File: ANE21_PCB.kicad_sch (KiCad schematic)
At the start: 23 parts, among them J1 Conn_02x07_Odd_Even, J2 Conn_01x03, J3 Conn_01x03, J4 THD-20-R, U1 74LVC1G07SE-7, U2 74LVC1G07SE-7

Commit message: Added footprints and symbols
Could not find -on SnapEDA- MCWR06X3322FTL, MCMR06X3162FTL and USB-A-S-VT.
Power load switch NCP380HSN05AAT1G only had footprint on SnapEDA, no symbol.
Need to update HMDI footprint and symbol to correct one.
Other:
- sheet CM4_GPIO ( Ethernet, GPIO, SDCARD) renamed Main
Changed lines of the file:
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@@
 			(color 255 255 255 0.0000)
 		)
-		(property "Sheetname" "CM4_GPIO ( Ethernet, GPIO, SDCARD)"
+		(property "Sheetname" "Main"
 			(at 213.36 127 0)
 			(effects

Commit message: Added footprints for PCIe and added busses for PCIe and Ethernet
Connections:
- net SYNC_IN: no longer Module?.16 (Ethernet_SYNC_IN(1.8v))
- net SYNC_OUT: no longer Module?.18 (Ethernet_SYNC_OUT(1.8v))
- no-connect marks 6 -> 8
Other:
- sheet Main renamed CM4_LowSpeed
- added sheet Ethernet (Ethernet.kicad_sch)

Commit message: Moved PCIe psu to global psu schematic
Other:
- removed sheet PCIe-connector
- sheet CM4_HighSpeed ports: added none; removed PCIE_CLK_N, PCIE_CLK_P, PCIE_CLK_nREQ, PCIE_RX_N, PCIE_RX_P, PCIE_TX_N, PCIE_TX_P, PCIE_nRST
- note added: "Connectors ------- Ethernet 40way RPI Jumpers"
- note added: "Connectors ------- HDMI 0 CSI 0 CSI 1"
- note removed: "Connector ------ PCIe x1"
- note removed: "Connectors ------- Ethernet SDCARD 40way RPI Jumpers"
- note removed: "Connectors ------- HDMI 0 HDMI 1 CSI 0 CSI 1 DSI 0 DSI 1"

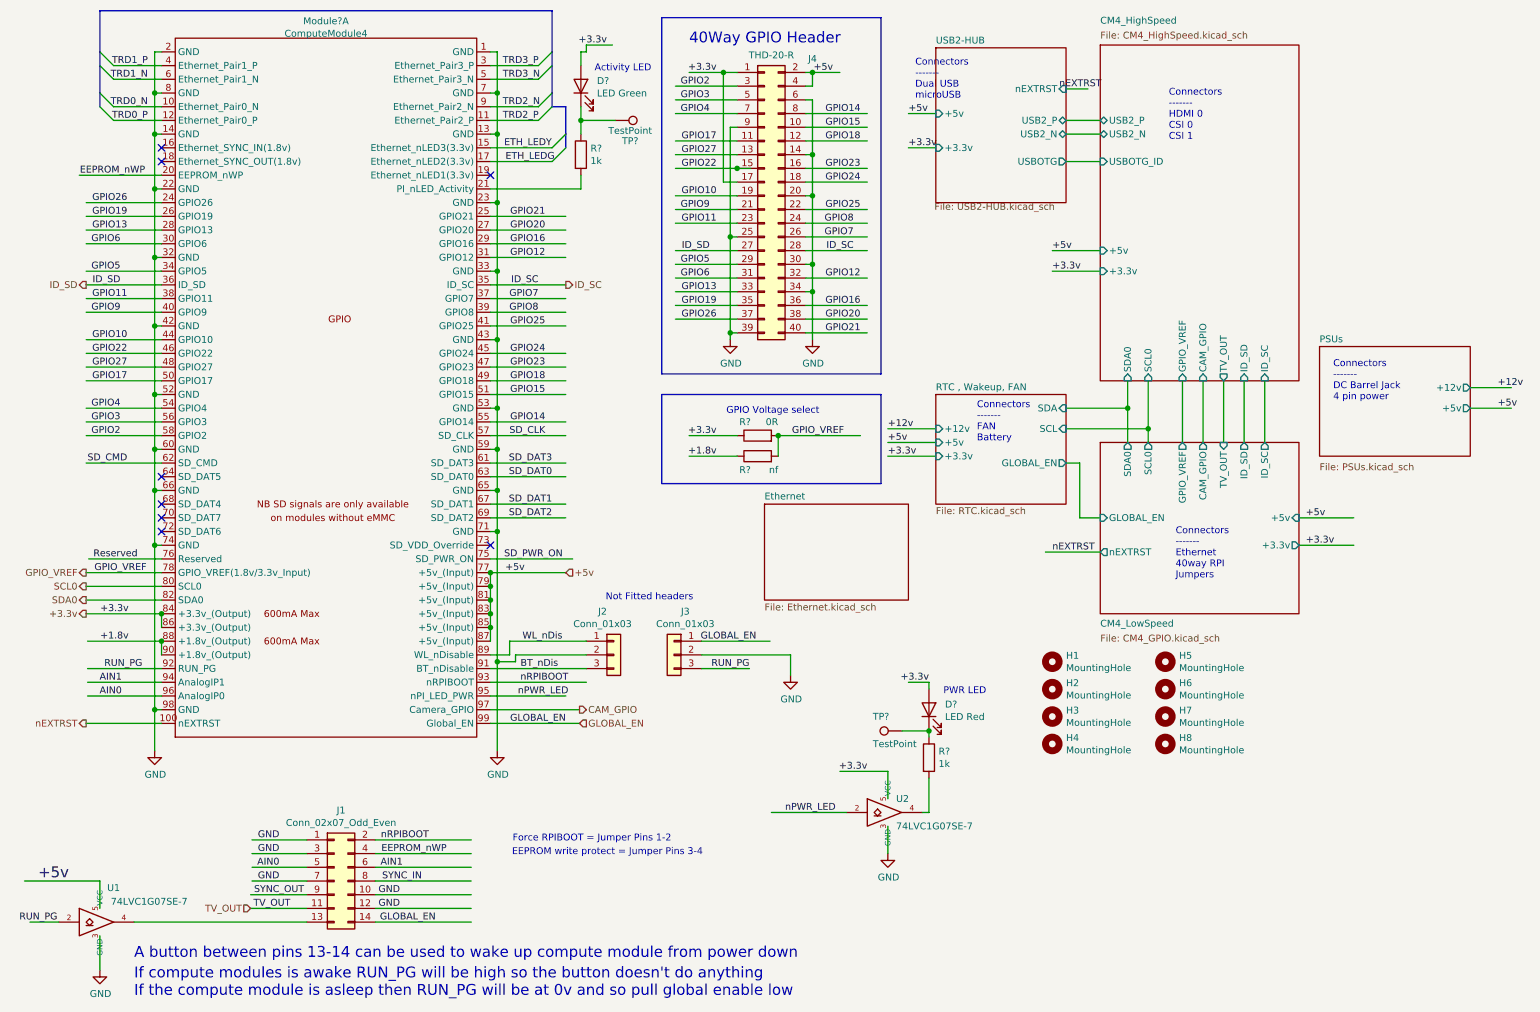
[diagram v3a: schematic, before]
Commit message: Cleaned up schematics and added gnds and no-connects
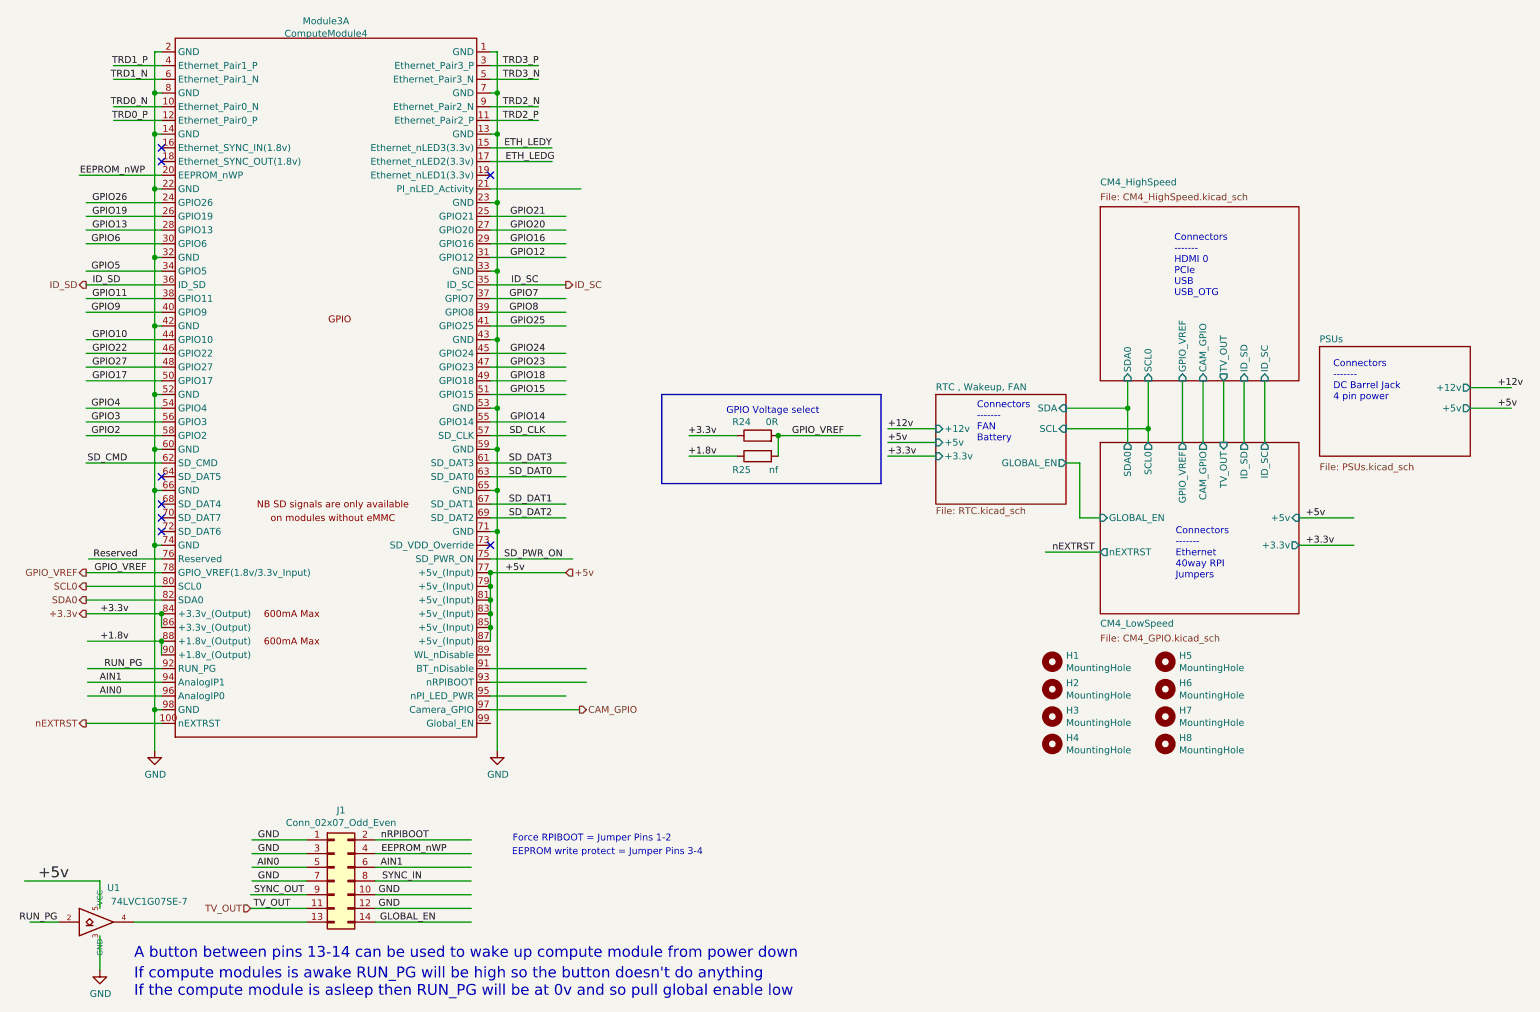
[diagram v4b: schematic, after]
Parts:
- removed D?: LED Green, LED_SMD:LED_0603_1608Metric, symbol Device:LED
- removed D?: LED Red, LED_SMD:LED_0603_1608Metric, symbol Device:LED
- removed J2, J3: Conn_01x03, Connector_PinHeader_2.54mm:PinHeader_1x03_P2.54mm_Vertical, symbol Connector_Generic:Conn_01x03
- removed J4: THD-20-R, Connector_PinHeader_2.54mm:PinHeader_2x20_P2.54mm_Vertical, symbol Connector_Generic:Conn_02x20_Odd_Even
- removed R? (x2): 1k, Resistor_SMD:R_0402_1005Metric, symbol Device:R
- removed TP? (x2): TestPoint, TestPoint:TestPoint_Pad_2.0x2.0mm, symbol Connector:TestPoint
- removed U2: 74LVC1G07SE-7, Package_TO_SOT_SMD:SOT-353_SC-70-5, symbol CM4IO:74LVC1G07_copy
- gave numbers to parts that had none: 3
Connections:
- net GLOBAL_EN: no longer Module3.99 (Global_EN)
- net nRPIBOOT: no longer Module3.93 (nRPIBOOT)
- net BT_nDis: no longer names the net of Module3.91 (BT_nDisable)
- net WL_nDis: no longer names the net of Module3.89 (WL_nDisable)
- net nPWR_LED: no longer names the net of Module3.95 (nPI_LED_PWR)
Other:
- removed sheet Ethernet
- removed sheet USB2-HUB
- sheet CM4_HighSpeed ports: added none; removed +3.3v, +5v, USB2_N, USB2_P, USBOTG_ID
- note added: "Connectors ------- HDMI 0 PCIe USB USB_OTG"
- note removed: "40Way GPIO Header"
- note removed: "Activity LED"
- note removed: "Connectors ------- Dual USB microUSB"
- note removed: "Connectors ------- HDMI 0 CSI 0 CSI 1"
- note removed: "Not Fitted headers"
- note removed: "PWR LED"

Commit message: Added 3d-models, esd protection, cleaned up and made small start with pcb
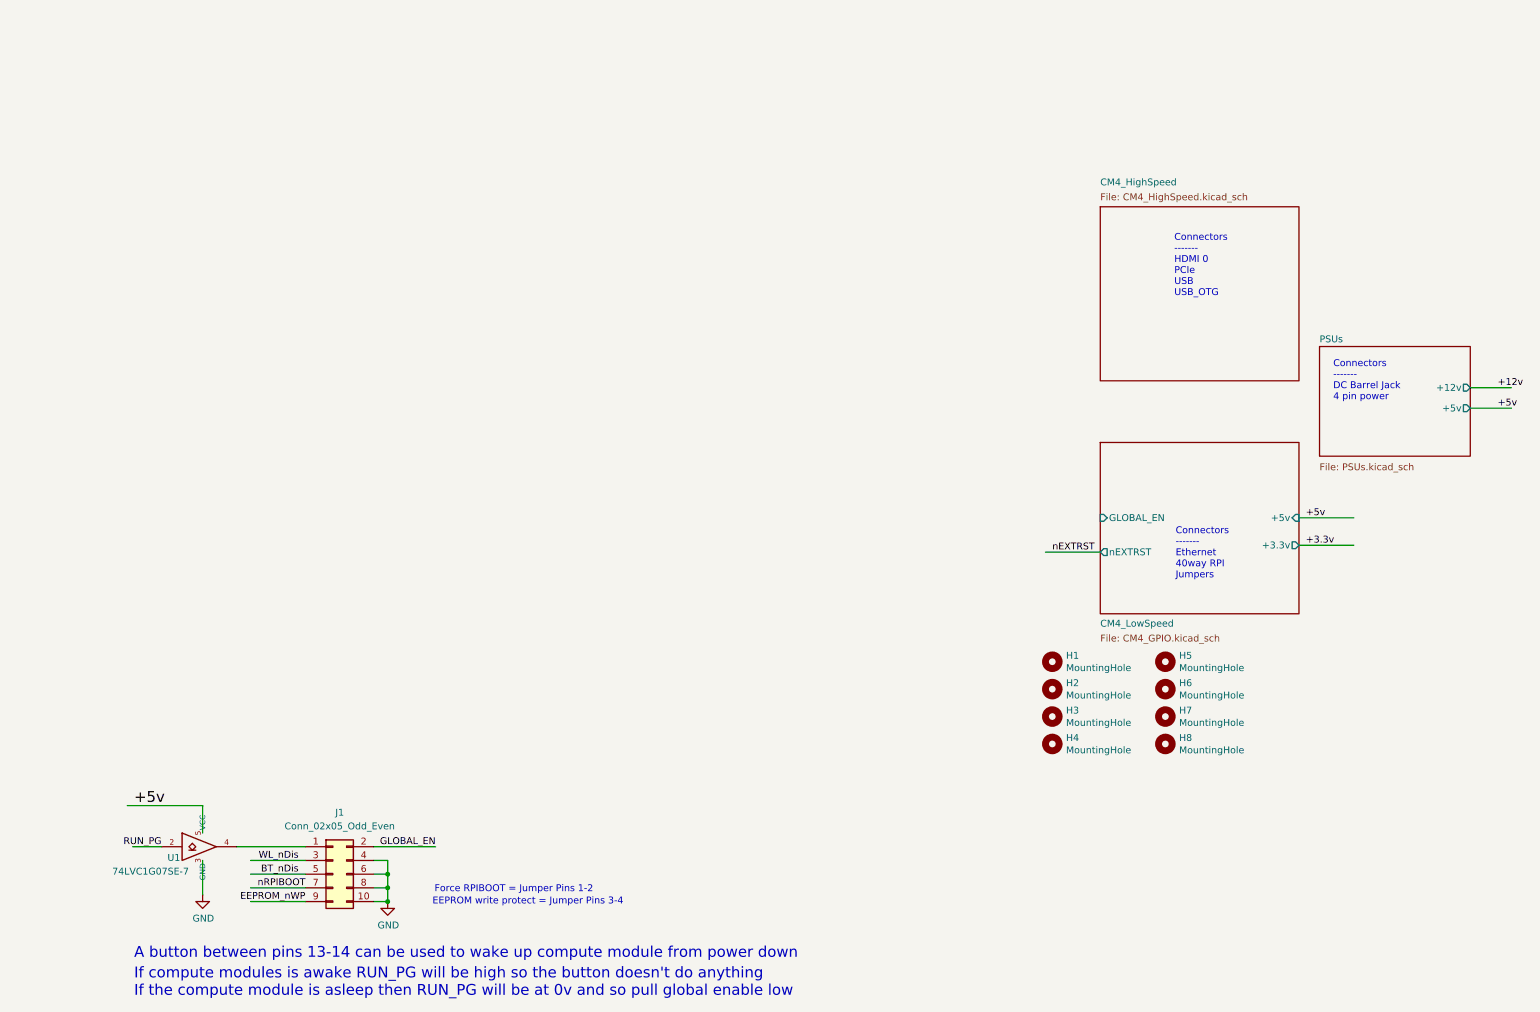
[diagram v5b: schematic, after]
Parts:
- removed J1: Conn_02x07_Odd_Even, Connector_PinHeader_2.54mm:PinHeader_2x07_P2.54mm_Vertical, symbol Connector_Generic:Conn_02x07_Odd_Even
- removed Module3: ComputeModule4, CM4IO:Raspberry-Pi-4-Compute-Module, symbol CM4IO:ComputeModule4-CM4
- removed R24: 0R, Resistor_SMD:R_0805_2012Metric_Pad1.15x1.40mm_HandSolder, symbol Device:R
- removed R25: nf, Resistor_SMD:R_0805_2012Metric_Pad1.15x1.40mm_HandSolder, symbol Device:R
- added J1: Conn_02x05_Odd_Even, symbol Connector_Generic:Conn_02x05_Odd_Even
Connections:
- net EEPROM_nWP: now also J1.9 (Pin_9)
- net GLOBAL_EN: now also J1.2 (Pin_2)
- net GND: now also J1.10 (Pin_10), J1.4 (Pin_4), J1.6 (Pin_6), J1.8 (Pin_8)
- net nRPIBOOT: now also J1.7 (Pin_7)
- net at U1.4: now also J1.1 (Pin_1)
- new net BT_nDis: J1.5 (Pin_5)
- new net WL_nDis: J1.3 (Pin_3)
- no-connect marks 8 -> 0
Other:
- removed sheet RTC , Wakeup, FAN
- sheet CM4_HighSpeed ports: added none; removed CAM_GPIO, GPIO_VREF, ID_SC, ID_SD, SCL0, SDA0, TV_OUT
- sheet CM4_LowSpeed ports: added none; removed CAM_GPIO, GPIO_VREF, ID_SC, ID_SD, SCL0, SDA0, TV_OUT
- note removed: "Connectors ------- FAN Battery"
- note removed: "GPIO Voltage select"
- moved on the sheet: U1

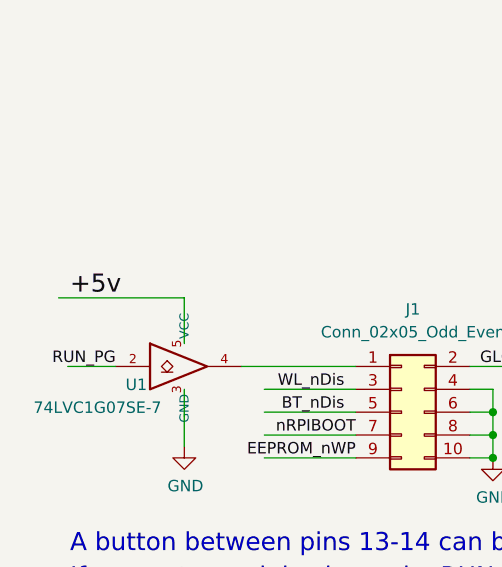
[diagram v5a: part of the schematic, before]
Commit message: heb de GPIO aangepast.
Laten we morgen de stand van zaken bespreken. En overleggen wat we kunnen doen
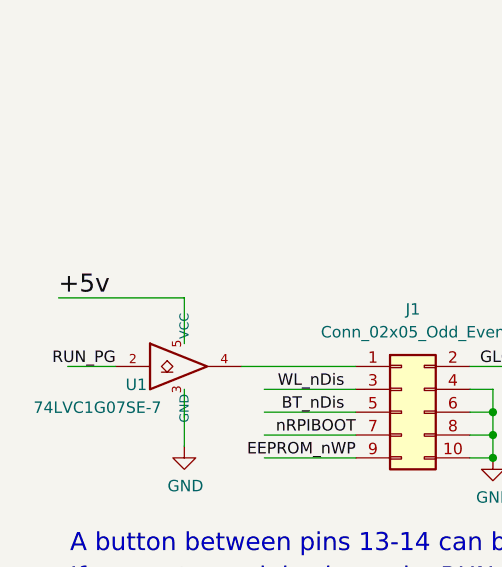
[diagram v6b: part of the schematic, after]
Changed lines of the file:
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@@
 	)
 	(label "+5v"
-		(at 34.29 160.02 0)
+		(at 33.02 160.02 0)
 		(effects
 			(font

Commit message: Commit
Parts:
- removed J1: Conn_02x05_Odd_Even, symbol Connector_Generic:Conn_02x05_Odd_Even
- removed U1: 74LVC1G07SE-7, Package_TO_SOT_SMD:SOT-353_SC-70-5, symbol CM4IO:74LVC1G07_copy
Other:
- note removed: "A button between pins 13-14 can be used to wake up compute module from power down"
- note removed: "EEPROM write protect = Jumper Pins 3-4"
- note removed: "Force RPIBOOT = Jumper Pins 1-2"
- note removed: "If compute modules is awake RUN_PG will be high so the button doesn't do anything If the compute module is asleep then RUN_PG will be at 0v and so pull global enable low"
